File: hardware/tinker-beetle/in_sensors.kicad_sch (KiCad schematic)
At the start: 27 parts, among them J8 CON-SMA-EDGE-S, U16 E220-900MM22S, U2 ISM6HG256XTR, U23 INA230AIRGTR, U3 QMC5883P, U4 BMP581, U5 LC86GLAMD

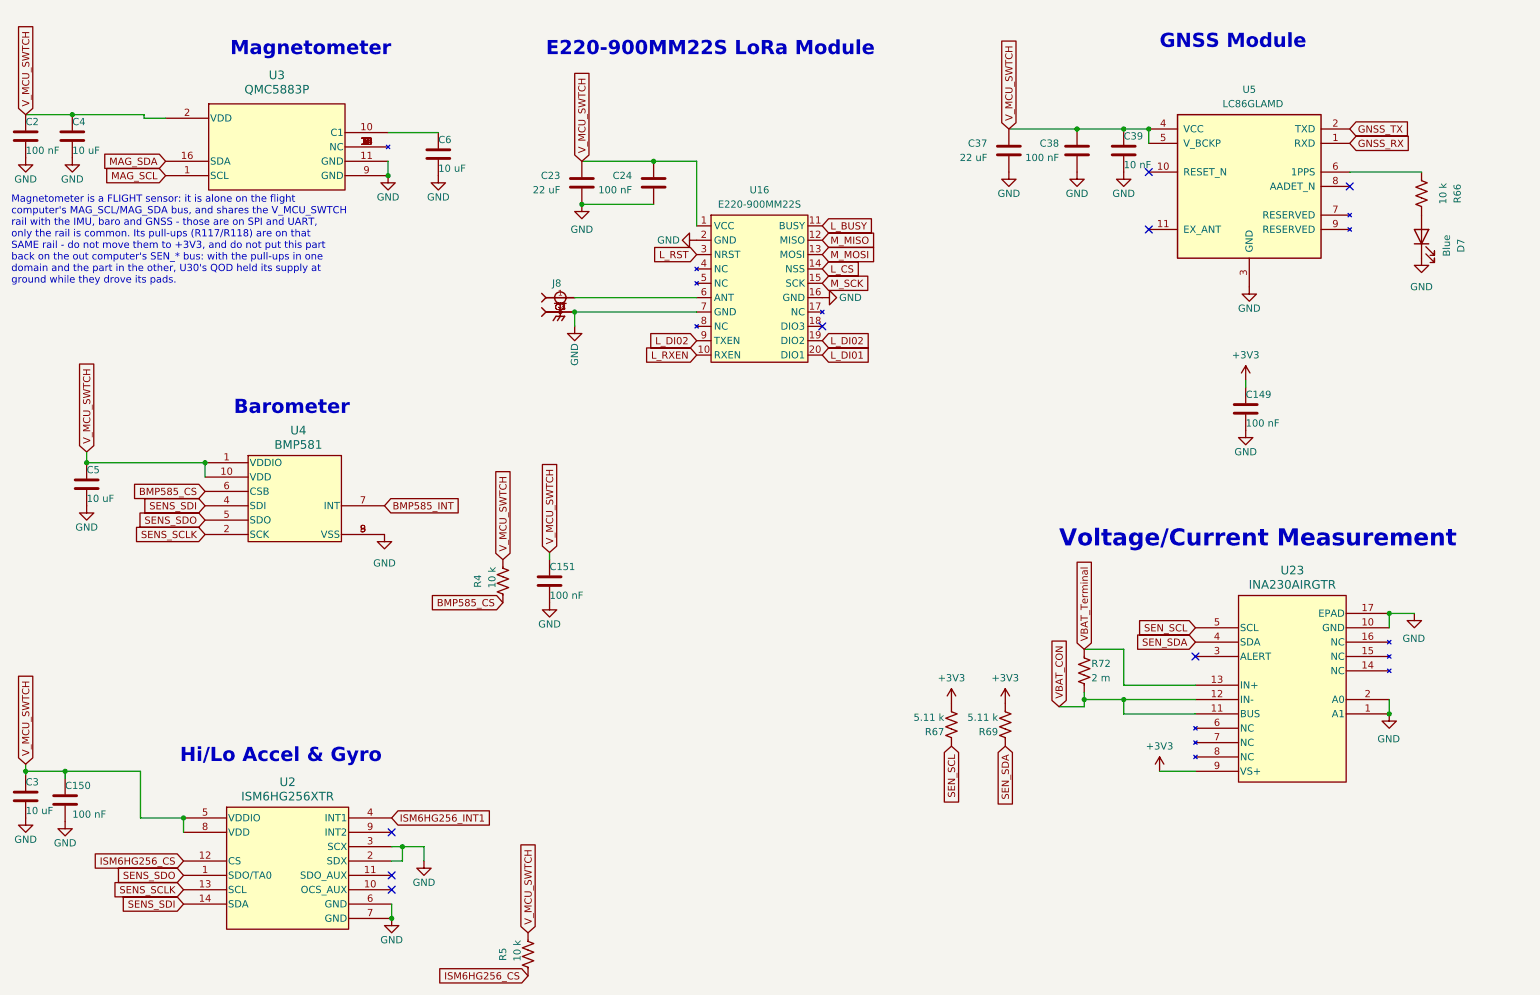
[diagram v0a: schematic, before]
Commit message: hardware(Tinker-Beetle V2, Tinker-Mantis V11, LoRa V4): the ESP32-S3s take their boot flash in the package, and the Beetle's V2 work to date (#1684)
Every in-work board's ESP32-S3RH2 + external W25Q128JVYIQ becomes an
ESP32-S3FH4R2 (4 MB quad flash + the same 2 MB quad PSRAM in the package,
same QFN-56 and pinout). The boot NOR and its 100 nF go; pads 30-35 carry
no-connect flags. The S3FN8 was not used: the Beetle FC's raw-GNSS filter
keeps ~219 KB in PSRAM and the OC's log ring is 512 KB there.

- Tinker-Beetle V2: U15/U32 -> FH4R2; U13, U33, C26, C115 removed.
- Tinker-Mantis V11: out computer U15 -> FH4R2; U13, C26 removed. The P4's
  boot flash U16 stays (no P4 has in-package flash).
- LoRa daughterboard V4: U28 -> FH4R2; U22, C18 removed. radio_board already
  declares 4 MB with PSRAM off, so its firmware needs no change.

The Beetle folder also carries the rest of its uncommitted V2 work, which
shares these files: TPS1HC08-Q1 eFuse pyro switches (U6-U8, U10, R144-R147;
Q3-Q6 gone), the PX1105R (U12) with its GVLB208.A antenna, the MMC5983MA
magnetometer on the sensor SPI, the Molex 0479480001 BLE antenna, the WAGO
2601-1105 battery terminal (J2), the SHOU HAN vertical USB-C (J6), no FC
32.768 kHz crystal (Y3), the BAT54XV2T1G power-switch OR (D9/D12) and the
BOM consolidation. The libraries gain the symbols and footprints those use
(MMC5983MA's GND pins become power inputs).

Checked: tools/check_board_parity.py passes on every board. ERC and
netlists match the working copy they came from. PCB DRC with schematic
parity: LoRa 0 unconnected, Mantis 4, Beetle 190 (its V2 layout is in
progress). Firmware for the 4 MB partition tables (Beetle V2, Mantis V11
OC) is not part of this.

Not included: Tinker-Base V2 (FH4R2 + U23 log flash, GCT USB4110-GF-A J2,
330 ohm LED resistors). Its PCB has not been updated yet, so it fails the
board-parity check.

Co-authored-by: Claude Opus 5.5 <noreply@anthropic.com>
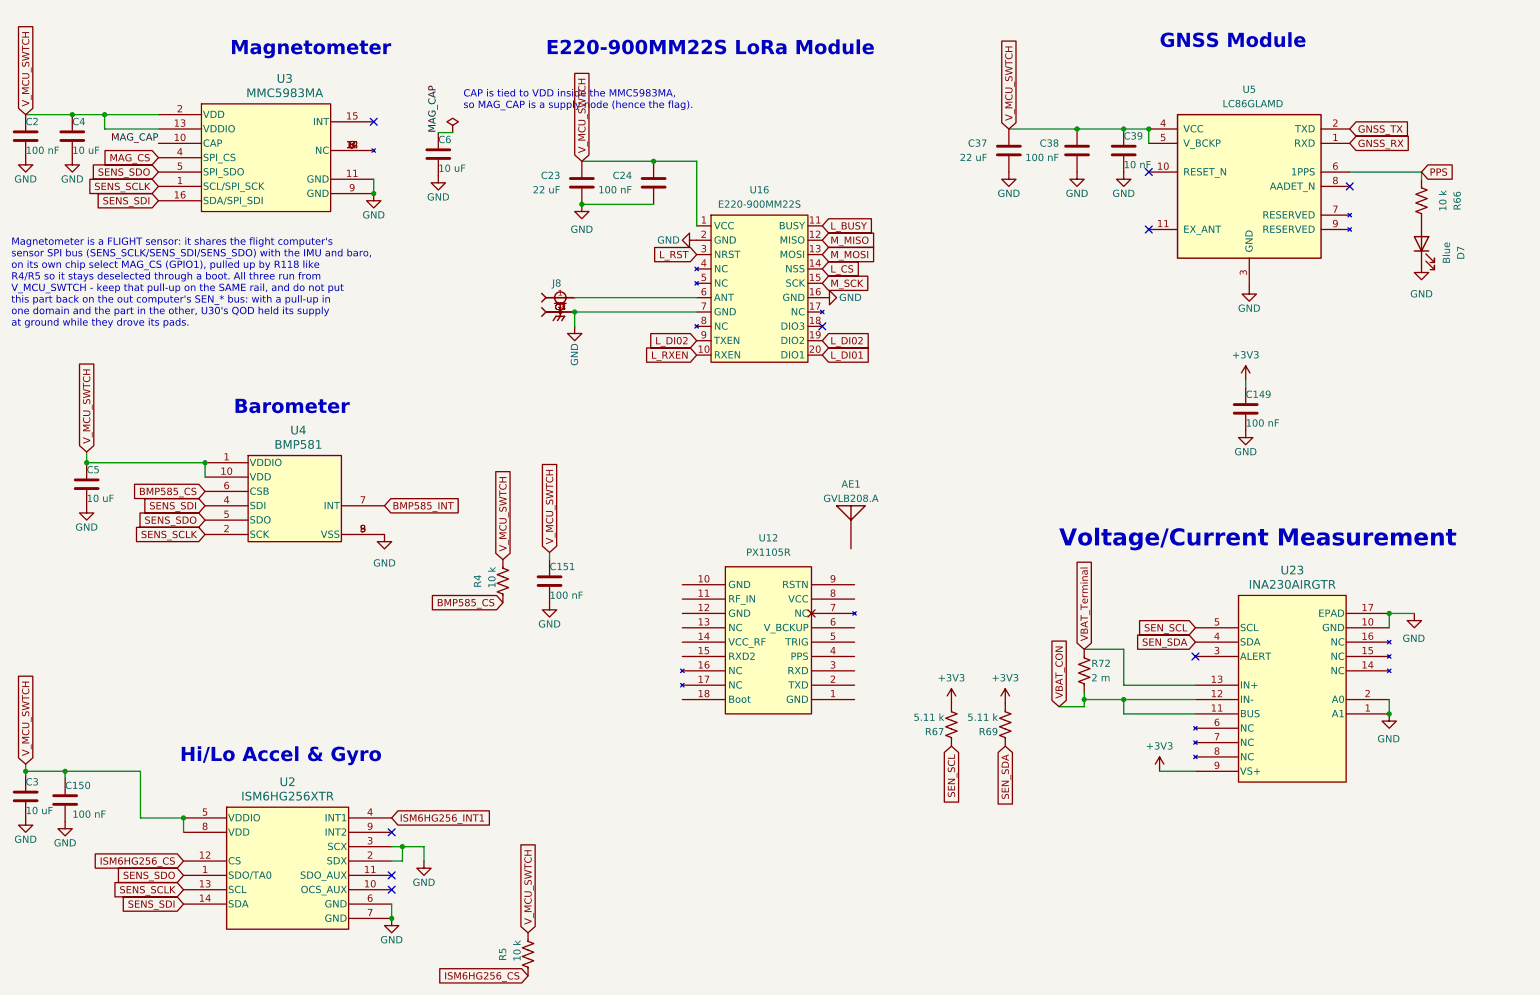
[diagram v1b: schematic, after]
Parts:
- added AE1: GVLB208.A, Footprints:ANT_GVLB208.A_TAOGLAS, symbol Custom:GVLB208.A
- added U12: PX1105R, Footprints:PX1105R, symbol Custom:PX1105R
- D7: MPN APHHS1005QBC/D -> XL-1005UBC; Mfr Kingbright -> Xinglight
- U3: value QMC5883P -> MMC5983MA; footprint Footprints:QMC5883P_LGA-16_3x3 -> Footprints:MMC5983MA_LGA-16_3x3; symbol Custom:QMC5883P -> Custom:MMC5983MA; MPN QMC5883P -> MMC5983MA; Mfr QST -> MEMSIC
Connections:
- net MAG_SCL is gone; now on net SENS_SCLK: U3.1 (SCL/SPI_SCK)
- net MAG_SDA is gone; now on net SENS_SDI: U3.16 (SDA/SPI_SDI)
- net SENS_SDO: now also U3.5 (SPI_SDO)
- net V_MCU_SWTCH: now also U3.13 (VDDIO)
- net PPS: now reaches R66.1, U5.6 (1PPS)
- net MAG_CAP: now reaches C6.1, U3.10 (CAP)
- net at U3.12 (NC), U3.14 (NC), U3.3 (NC)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: no longer U3.13 (NC), U3.15 (NC), U3.4 (NC), U3.5 (NC)
- new net MAG_CS: U3.4 (SPI_CS)
- no-connect marks 8 -> 9
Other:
- note added: "CAP is tied to VDD inside the MMC5983MA, so MAG_CAP is a supply node (hence the flag)."
- note added: "Magnetometer is a FLIGHT sensor: it shares the flight computer's sensor SPI bus (SENS_SCLK/SENS_SDI/SENS_SDO) with the IMU and baro, on its own chip select MAG_CS (GPIO1), pulled up by R118 like R4/R5 so it stays deselected through a boot. All three run from V_MCU_SWTCH - keep that pull-up on the SAME rail, and do not put this part back on the out computer's SEN_* bus: with a pull-up in one domai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"
- note removed: "Magnetometer is a FLIGHT sensor: it is alone on the flight computer's MAG_SCL/MAG_SDA bus, and shares the V_MCU_SWTCH rail with the IMU, baro and GNSS - those are on SPI and UART, only the rail is common. Its pull-ups (R117/R118) are on that SAME rail - do not move them to +3V3, and do not put this part back on the out computer's SEN_* bus: with the pull-ups in one domain and the part in the othe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"
- moved on the sheet: D7, R66
